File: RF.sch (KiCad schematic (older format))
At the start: 24 parts

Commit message: a
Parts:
- added C204, C205, C207: 10n, symbol Device:C_Small
- added C208, C215: 100n, symbol Device:C_Small
- added L201: L, symbol Device:L
- added Q201: 2N7002, Package_TO_SOT_SMD:SOT-23, symbol Transistor_FET:2N7002
- added Q202: IRLML2060, Package_TO_SOT_SMD:SOT-23, symbol Transistor_FET:IRLML2060
- added R206: 50, symbol Device:R
- added R207, R208: 1k, symbol Device:R
- added R209, R210: 10k, symbol Device:R
- gave numbers to parts that had none: 22
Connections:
- net GND: now also C207.2, C208.2, C215.2, Q202.2 (S), R207.2, R210.2
- net VCC: now also R209.1
- net at U202.9 (2A): now also C205.1, R208.1
- net at R213.1, U201.2 (-): now also C214.2, R215.2
- new net: C208.1, R208.2, R209.2, R210.1
- new net: C205.2, R206.1
- new net: Q201.2 (S), R206.2, R207.1
- new net: C204.1, Q201.3 (D)
- new net: L201.2, Q202.3 (D)
- new net +12V: C215.1, L201.1
- new net RX: C207.1, Q201.1 (G)
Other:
- moved on the sheet: C201, C203, C206, C209, C210, C211, C212, C213, C214, R201, R202, R203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

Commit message: filter backup
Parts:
- added C?: 10u, symbol Device:C_Small
- added C? (x2): 10n, symbol Device:C_Small
- added C?: 100n, symbol Device:C_Small
- added J1: Conn_Coaxial, symbol Connector:Conn_Coaxial
- added R? (x2): 10k, symbol Device:R
- added U1: Filter, uSDX:Filter, symbol uSDX:Filter
- added U?: 74AHCT1G00, symbol 74xGxx:74AHCT1G00
- L201: value L -> FT-37-43
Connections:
- net +12V: now also C?.1
- net GND: now also C?.2, C?.2, C?.2, J1.2 (Ext), U1.3 (GND), U?.3 (GND)
- net VCC: now also C?.1, U?.5 (VCC)
- net at C204.2: now also L201.2, Q202.3 (D), U1.1 (IN)
- net at Q202.1 (G): now also C?.1, R?.1
- net CLK0 renamed CLK_I
- net CLK1 renamed CLK_Q
- new net: J1.1 (In), U1.2 (OUT)
- new net: C?.2, U?.4
- new net: C?.1, R?.1, R?.2
- new net KEY_PWM: R?.2
- new net TX_CLK: U?.1, U?.2
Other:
- moved on the sheet: C215, L201, Q202

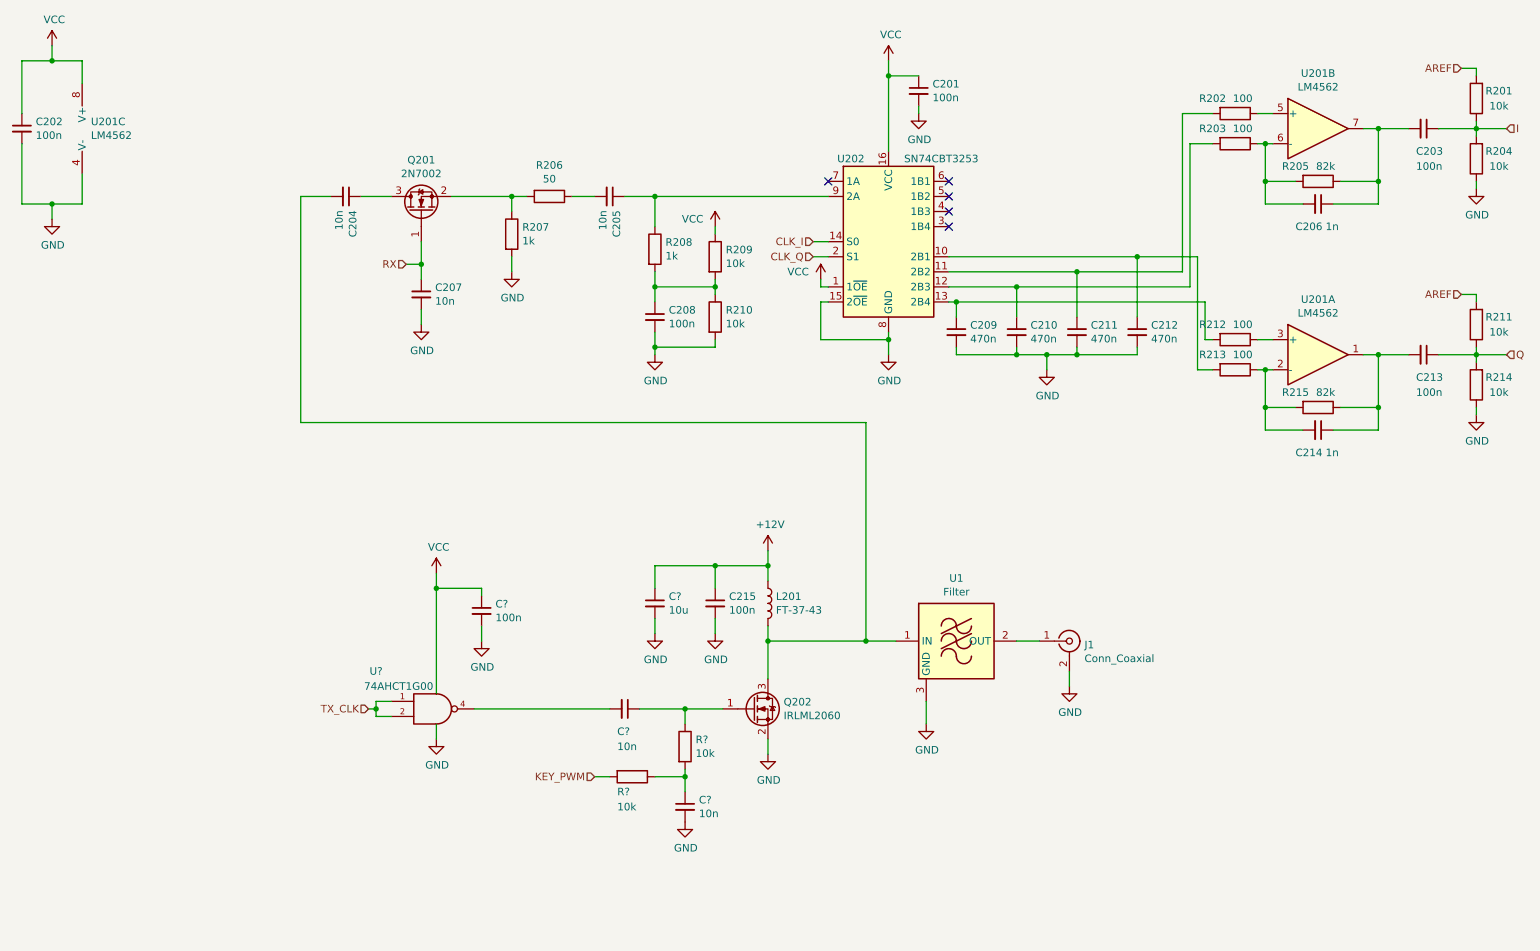
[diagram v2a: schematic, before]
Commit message: PCB in progress, filter screwed up
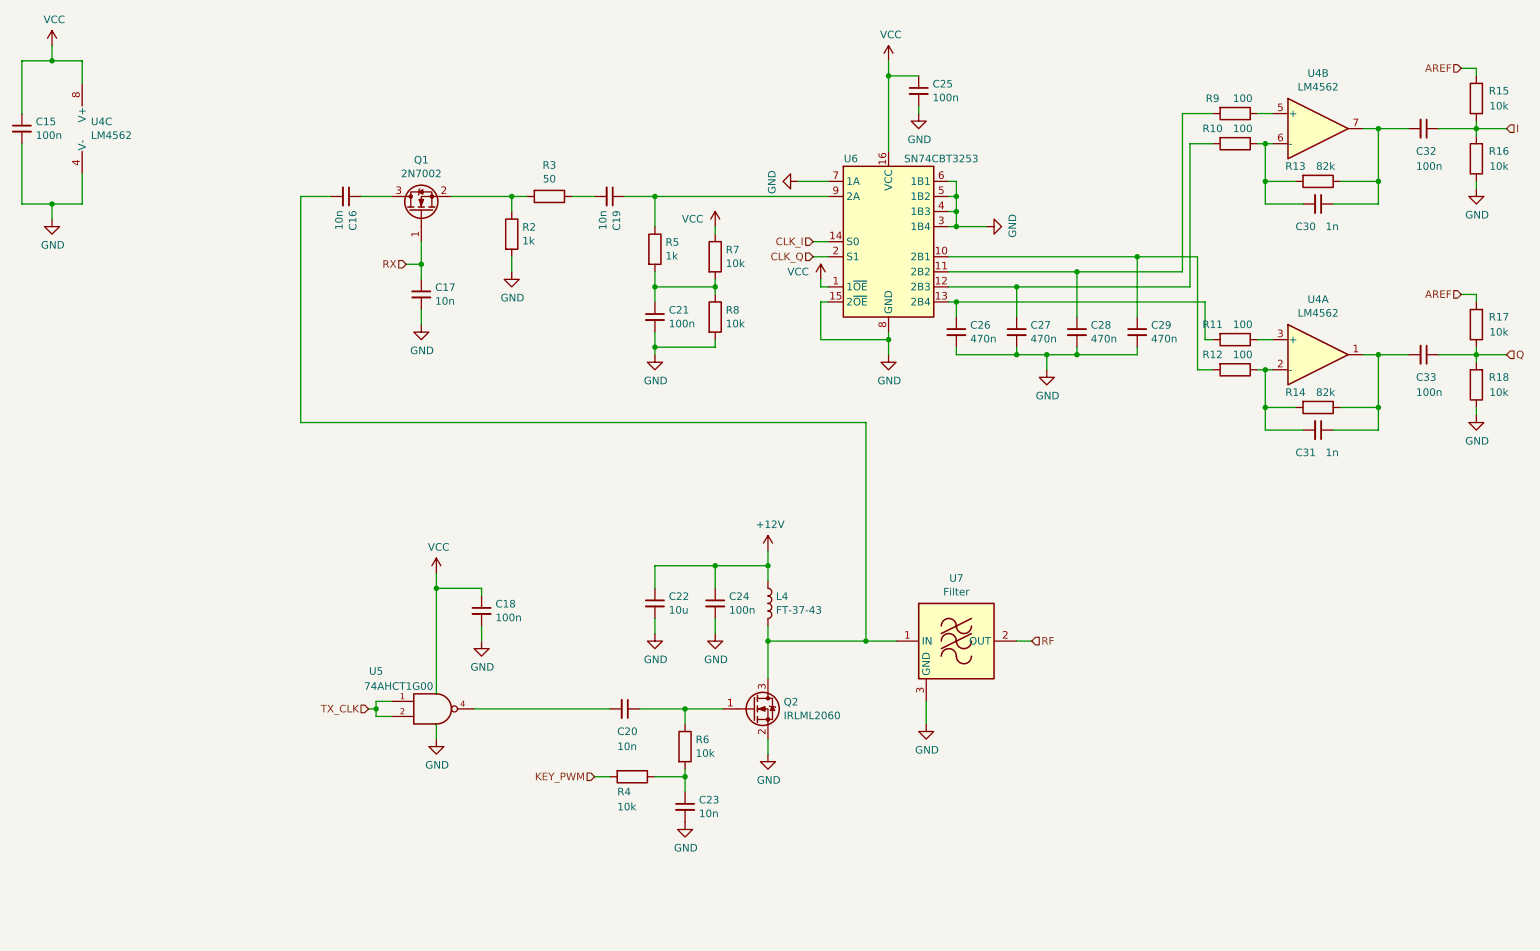
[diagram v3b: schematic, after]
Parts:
- removed J1: Conn_Coaxial, symbol Connector:Conn_Coaxial
- C15: renamed from C202; footprint (none) -> Capacitor_SMD:C_0805_2012Metric_Pad1.18x1.45mm_HandSolder
- C16: renamed from C204; footprint (none) -> Capacitor_SMD:C_0805_2012Metric_Pad1.18x1.45mm_HandSolder
- C17: renamed from C207; footprint (none) -> Capacitor_SMD:C_0805_2012Metric_Pad1.18x1.45mm_HandSolder
- C18, C20, C22, C23: renamed from C?; footprint (none) -> Capacitor_SMD:C_0805_2012Metric_Pad1.18x1.45mm_HandSolder
- C19: renamed from C205; footprint (none) -> Capacitor_SMD:C_0805_2012Metric_Pad1.18x1.45mm_HandSolder
- C21: renamed from C208; footprint (none) -> Capacitor_SMD:C_0805_2012Metric_Pad1.18x1.45mm_HandSolder
- C24: renamed from C215; footprint (none) -> Capacitor_SMD:C_0805_2012Metric_Pad1.18x1.45mm_HandSolder
- C25: renamed from C201; footprint (none) -> Capacitor_SMD:C_0805_2012Metric_Pad1.18x1.45mm_HandSolder
- C26: renamed from C209; footprint (none) -> Capacitor_SMD:C_0805_2012Metric_Pad1.18x1.45mm_HandSolder
- C27: renamed from C210; footprint (none) -> Capacitor_SMD:C_0805_2012Metric_Pad1.18x1.45mm_HandSolder
- C28: renamed from C211; footprint (none) -> Capacitor_SMD:C_0805_2012Metric_Pad1.18x1.45mm_HandSolder
- C29: renamed from C212; footprint (none) -> Capacitor_SMD:C_0805_2012Metric_Pad1.18x1.45mm_HandSolder
- C30: renamed from C206; footprint (none) -> Capacitor_SMD:C_0805_2012Metric_Pad1.18x1.45mm_HandSolder
- C31: renamed from C214; footprint (none) -> Capacitor_SMD:C_0805_2012Metric_Pad1.18x1.45mm_HandSolder
- C32: renamed from C203; footprint (none) -> Capacitor_SMD:C_0805_2012Metric_Pad1.18x1.45mm_HandSolder
- C33: renamed from C213; footprint (none) -> Capacitor_SMD:C_0805_2012Metric_Pad1.18x1.45mm_HandSolder
- L4: renamed from L201; footprint (none) -> Inductor_THT:L_Toroid_Horizontal_D9.5mm_P15.00mm_Diameter10-5mm_Amidon-T37
- R10: renamed from R203; footprint (none) -> Resistor_SMD:R_0805_2012Metric_Pad1.20x1.40mm_HandSolder
- R11: renamed from R212; footprint (none) -> Resistor_SMD:R_0805_2012Metric_Pad1.20x1.40mm_HandSolder
- R12: renamed from R213; footprint (none) -> Resistor_SMD:R_0805_2012Metric_Pad1.20x1.40mm_HandSolder
- R13: renamed from R205; footprint (none) -> Resistor_SMD:R_0805_2012Metric_Pad1.20x1.40mm_HandSolder
- R14: renamed from R215; footprint (none) -> Resistor_SMD:R_0805_2012Metric_Pad1.20x1.40mm_HandSolder
- R15: renamed from R201; footprint (none) -> Resistor_SMD:R_0805_2012Metric_Pad1.20x1.40mm_HandSolder
- R16: renamed from R204; footprint (none) -> Resistor_SMD:R_0805_2012Metric_Pad1.20x1.40mm_HandSolder
- R17: renamed from R211; footprint (none) -> Resistor_SMD:R_0805_2012Metric_Pad1.20x1.40mm_HandSolder
- R18: renamed from R214; footprint (none) -> Resistor_SMD:R_0805_2012Metric_Pad1.20x1.40mm_HandSolder
- R2: renamed from R207; footprint (none) -> Resistor_SMD:R_0805_2012Metric_Pad1.20x1.40mm_HandSolder
- R3: renamed from R206; footprint (none) -> Resistor_SMD:R_0805_2012Metric_Pad1.20x1.40mm_HandSolder
- R4, R6: renamed from R?; footprint (none) -> Resistor_SMD:R_0805_2012Metric_Pad1.20x1.40mm_HandSolder
- R5: renamed from R208; footprint (none) -> Resistor_SMD:R_0805_2012Metric_Pad1.20x1.40mm_HandSolder
- R7: renamed from R209; footprint (none) -> Resistor_SMD:R_0805_2012Metric_Pad1.20x1.40mm_HandSolder
- R8: renamed from R210; footprint (none) -> Resistor_SMD:R_0805_2012Metric_Pad1.20x1.40mm_HandSolder
- R9: renamed from R202; footprint (none) -> Resistor_SMD:R_0805_2012Metric_Pad1.20x1.40mm_HandSolder
- U4: renamed from U201; footprint (none) -> Package_SO:SOIC-8_3.9x4.9mm_P1.27mm
- U5: renamed from U?; footprint (none) -> Package_TO_SOT_SMD:SOT-23-5_HandSoldering
- U6: renamed from U202; footprint (none) -> Package_SO:SOIC-16_3.9x9.9mm_P1.27mm
- renumbered Q201 to Q1, Q202 to Q2, U1 to U7
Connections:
- net GND: now also U6.3 (1B4), U6.4 (1B3), U6.5 (1B2), U6.6 (1B1), U6.7 (1A)
- net RF: now reaches U7.2 (OUT)
- no-connect marks 5 -> 0

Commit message: Work on PCB
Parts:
- added Q5, Q6: IRLML2060, Package_TO_SOT_SMD:SOT-23, symbol Transistor_FET:IRLML2060
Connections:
- net GND: now also Q5.2 (S), Q6.2 (S)
- net at C16.2, L4.2, Q2.3 (D)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: now also Q5.3 (D), Q6.3 (D)
- net at C20.1, Q2.1 (G), R6.1: now also Q5.1 (G), Q6.1 (G)
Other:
- moved on the sheet: C18, C20, C23, R4, R6, U5
